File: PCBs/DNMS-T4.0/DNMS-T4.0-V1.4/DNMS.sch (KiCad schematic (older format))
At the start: 14 parts, among them J1 Conn_01x02, J2 Conn_02x03_Odd_Even, J3 Conn_01x04, J4 Conn_01x01, J5 RJ12, J6 RJ12, U1 Teensy4.0, U2 P82B715PN,112, U3 P82B715DR

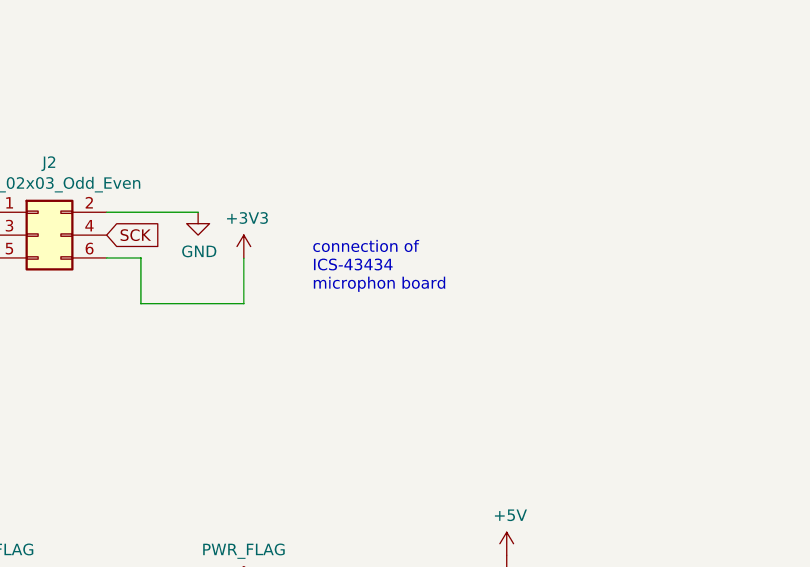
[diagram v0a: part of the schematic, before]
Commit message: spelling changes
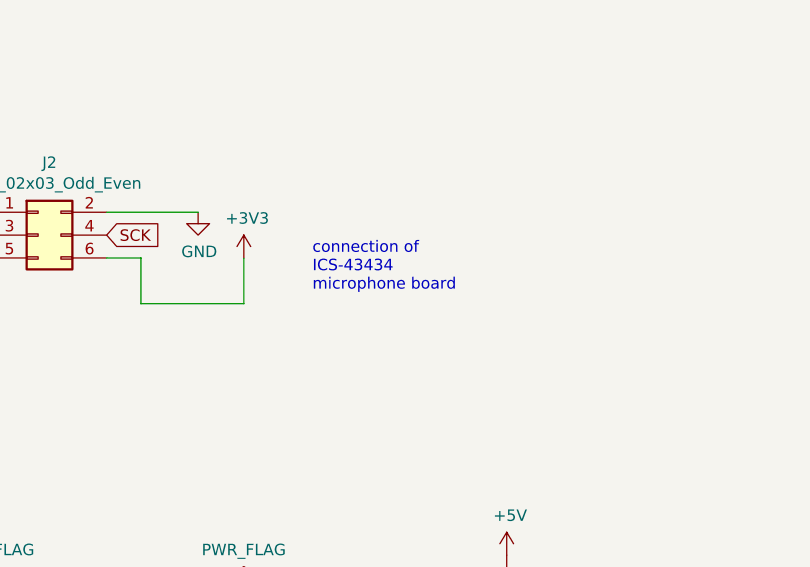
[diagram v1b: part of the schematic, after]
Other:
- note added: "connection of\nICS-43434\nmicrophone board"
- note removed: "connection of\nICS-43434\nmicrophon board"
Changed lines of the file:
@@
 I²C\nconnection
 Text Notes 4650 5250 0    50   ~ 0
-connection of\nICS-43434\nmicrophon board
+connection of\nICS-43434\nmicrophone board
 Wire Wire Line
 	7100 1850 7350 1850
